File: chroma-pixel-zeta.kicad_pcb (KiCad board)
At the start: 4 copper layers, 138 x 93.2 mm, 181 parts, among them J10 Conn_01x24_MountingPin, J11 AudioJack3, J12 USB_A, J14 LCD_TP_I2C, J2 TFT_LCD, J3 2169900003, J4 SPI_LCD, J5 I2C-STEMMA-QT, J6 Micro_SD_Card_Det1, J7 swd, J8 SPKR, J9 UART, Q1 MMBT3904, Q2 MMBT3904, Q3 MMBT3904, SW1 SW_Push, SW2 SW_Push, SW3 SW_Push, SW4 SW_Push, U1 MT25Q, U10 PCM5102A, U11 TLV75733PDBV, U12 STMPS2141STR, U2 STM32H743IITx, U4 MT25Q, U5 TPS61169, U6 MAX98357AETE_, U7 CAT24C128, U8 TLV75733PDBV, U9 MT48LC16M16A2P, Y1 25MHz, Y2 32.768KHz

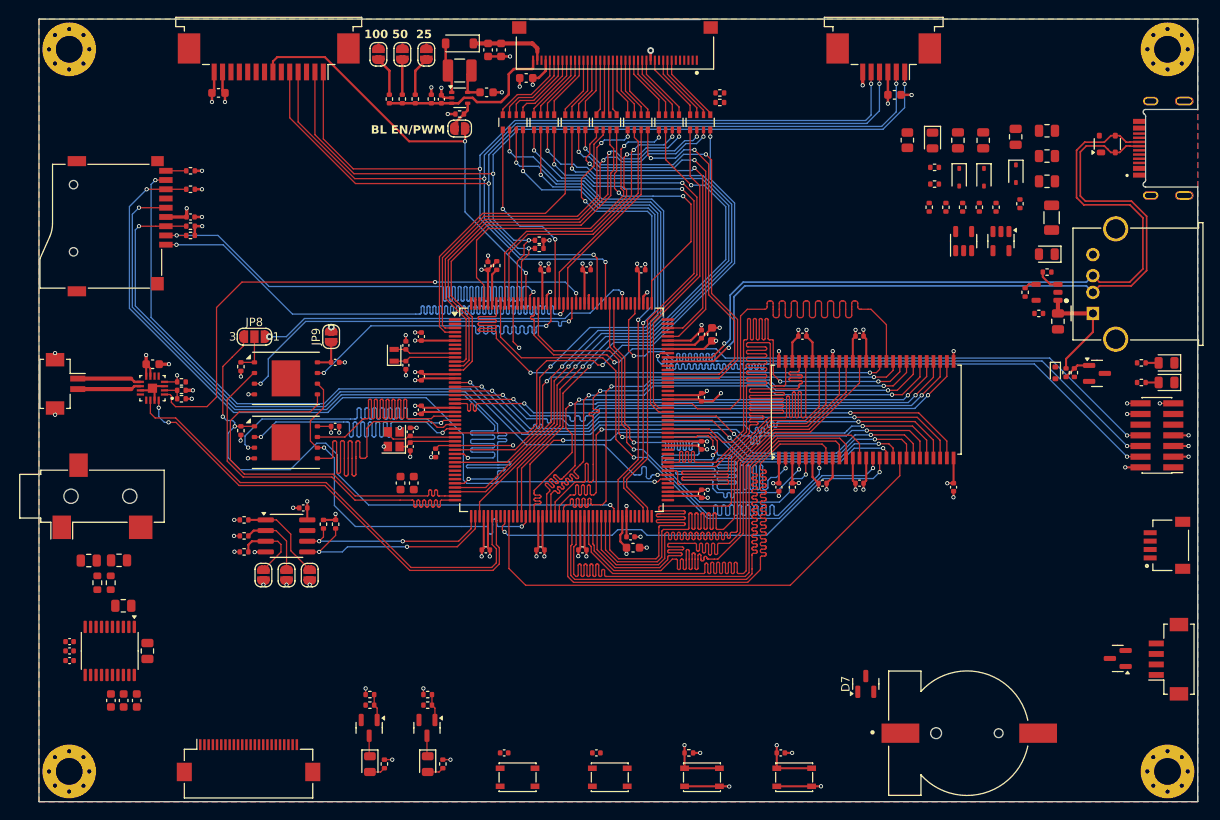
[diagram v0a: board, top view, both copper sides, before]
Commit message: Button, LED, i2s audio, LCD & SD ctrl left
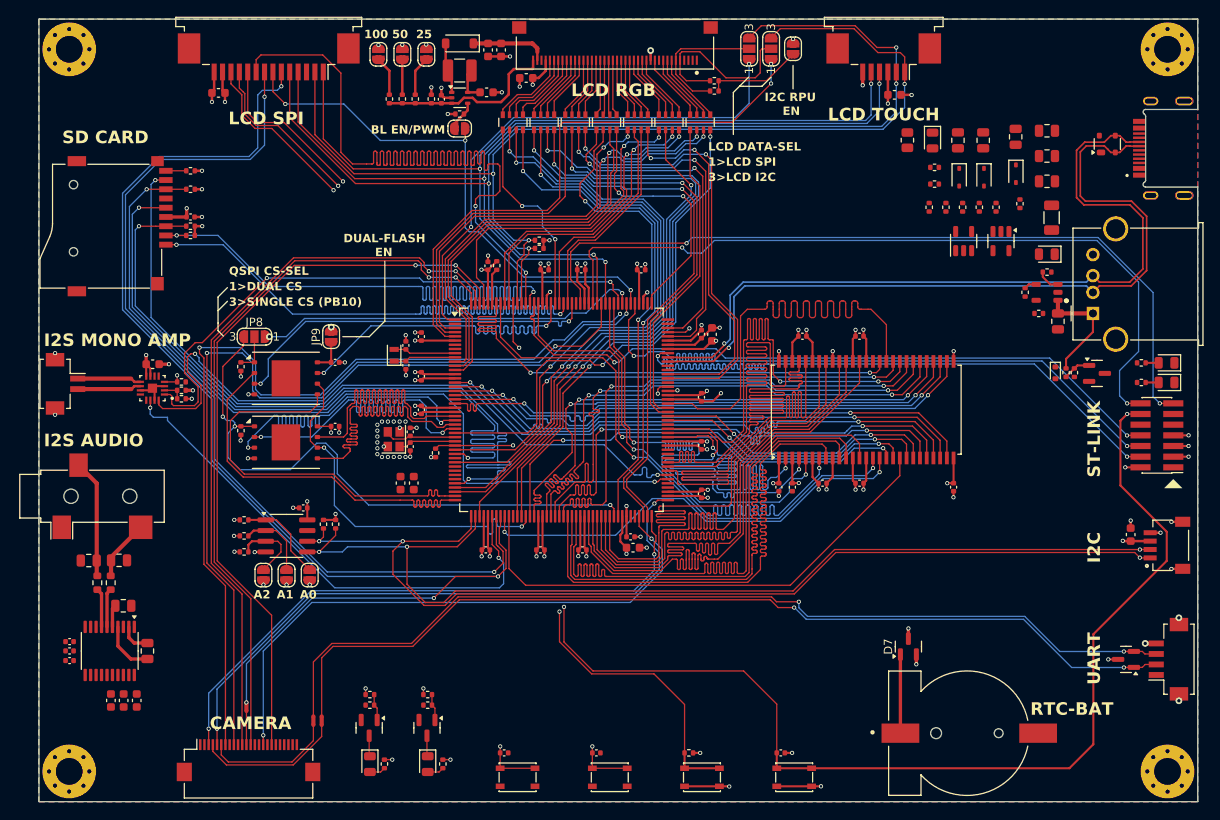
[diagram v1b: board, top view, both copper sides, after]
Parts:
- added C67: 10u, Capacitor_SMD:C_0603_1608Metric, F.Cu at (210.3, 108.4)
- added JP12: JMP, Jumper:SolderJumper-2_P1.3mm_Open_RoundedPad1.0x1.5mm, F.Cu at (170.1, 50.6)
- added JP13: LCD_DAT_SEL, Jumper:SolderJumper-3_P1.3mm_Open_RoundedPad1.0x1.5mm_NumberLabels, F.Cu at (167.4, 50.6)
- added JP14: LCD_CLK_SEL, Jumper:SolderJumper-3_P1.3mm_Open_RoundedPad1.0x1.5mm_NumberLabels, F.Cu at (164.8, 50.6)
- added NT1: NetTie_2, NetTie:NetTie-2_SMD_Pad0.5mm, F.Cu at (105.0, 128.9)
- added NT2: NetTie_2, NetTie:NetTie-2_SMD_Pad0.5mm, F.Cu at (112.9, 130.6)
- added NT3: NetTie_2, NetTie:NetTie-2_SMD_Pad0.5mm, F.Cu at (113.9, 130.6)
- moved D7 6.75 mm to (183.8, 121.8)
- moved R35 2.67 mm to (160.7, 54.4)
- moved D9 0.99 mm to (209.7, 123.3)
- moved R36 0.69 mm to (160.7, 55.6)
- moved C13 0.64 mm to (144.8, 76.9)
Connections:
- net /LCD/LCD_SCL renamed /LCD/LCD_CLK
- net /LCD/LCD_SDA renamed /LCD/LCD_DAT
- D9 pad 1: /IO/USART2_RX -> /IO/USART6_RX
- D9 pad 2: /IO/USART2_TX -> /IO/USART6_TX
- J10 pad 11: unconnected-(J10-Pin_11-Pad11) -> /DCMI/DCMI_D6
- J10 pad 12: /DCMI/DCMI_D7 -> /DCMI/DCMI_PIXCLK
- J10 pad 13: /DCMI/DCMI_PIXCLK -> /DCMI/DCMI_D7
- J10 pad 14: /DCMI/DCMI_D6 -> unconnected-(J10-Pin_14-Pad14)
- J10 pad 16: /DCMI/DCMI_D5 -> /DCMI/DCMI_HSYNC
- J10 pad 18: /DCMI/DCMI_D4 -> /DCMI/DCMI_VSYNC
- J10 pad 19: /DCMI/DCMI_D0 -> unconnected-(J10-Pin_19-Pad19)
- J10 pad 20: /DCMI/DCMI_D3 -> unconnected-(J10-Pin_20-Pad20)
- J10 pad 21: /DCMI/DCMI_D1 -> unconnected-(J10-Pin_21-Pad21)
- J10 pad 22: /DCMI/DCMI_D2 -> unconnected-(J10-Pin_22-Pad22)
- J10 pad 3: unconnected-(J10-Pin_3-Pad3) -> /DCMI/DCMI_D2
- J10 pad 4: unconnected-(J10-Pin_4-Pad4) -> /DCMI/DCMI_D1
- J10 pad 5: unconnected-(J10-Pin_5-Pad5) -> /DCMI/DCMI_D3
- J10 pad 6: unconnected-(J10-Pin_6-Pad6) -> /DCMI/DCMI_D0
- J10 pad 7: /DCMI/DCMI_VSYNC -> /DCMI/DCMI_D4
- J10 pad 9: /DCMI/DCMI_HSYNC -> /DCMI/DCMI_D5
- J4 pad 11: /LCD/LCD_RESET -> /LCD/LCD_SPI_RESET
- J9 pad 2: /IO/USART2_RX -> /IO/USART6_RX
- J9 pad 3: /IO/USART2_TX -> /IO/USART6_TX
- R31 pad 2: /MEMORY EEPROM/SDA -> /IO/STEMMA_SDA
- R32 pad 2: /MEMORY EEPROM/SCL -> /IO/STEMMA_SCL
- R35 pad 1: +3V3 -> Net-(JP12-A)
- R36 pad 1: +3V3 -> Net-(JP12-A)
- U2 pad 1: unconnected-(U2-PE2-Pad1) -> /LCD/LCD_SPI_CLK
- U2 pad 115: unconnected-(U2-PC6-Pad115) -> /IO/USART6_TX
- U2 pad 116: unconnected-(U2-PC7-Pad116) -> /IO/USART6_RX
- U2 pad 129: unconnected-(U2-PH14-Pad129) -> /MCU/DCMI_D4
- U2 pad 131: unconnected-(U2-PI0-Pad131) -> /LCD/LCD_DISP
- U2 pad 132: unconnected-(U2-PI1-Pad132) -> /LCD/LCD_CS
- U2 pad 138: /AUDIO/LRCK -> /LCD/LCD_BLK
- U2 pad 139: /AUDIO/BCK -> /AUDIO/I2S_CK
- U2 pad 141: unconnected-(U2-PC12-Pad141) -> /AUDIO/I2S_SDO
- U2 pad 145: unconnected-(U2-PD3-Pad145) -> /MCU/DCMI_D5
- U2 pad 147: unconnected-(U2-PD5-Pad147) -> /IO/DBG_TX
- U2 pad 150: unconnected-(U2-PD6-Pad150) -> /IO/DBG_RX
- U2 pad 151: /AUDIO/I2S_SDO -> /LCD/LCD_SPI_RESET
- U2 pad 163: /LCD/LCD_BLK -> /LCD/LCD_SDI(MOSI)
- U2 pad 174: unconnected-(U2-PI5-Pad174) -> /DCMI/DCMI_VSYNC
- U2 pad 175: unconnected-(U2-PI6-Pad175) -> /MCU/DCMI_D6
- U2 pad 176: unconnected-(U2-PI7-Pad176) -> /MCU/DCMI_D7
- U2 pad 2: unconnected-(U2-PE3-Pad2) -> /MCU/SD_DET
- U2 pad 45: /MEMORY EEPROM/SCL -> /IO/STEMMA_SCL
- U2 pad 46: /MEMORY EEPROM/SDA -> /IO/STEMMA_SDA
- U2 pad 5: unconnected-(U2-PE6-Pad5) -> /LCD/LCD_SPI_DAT
- U2 pad 51: /AUDIO/I2S_CK -> /LCD/LCD_SCK
- U2 pad 52: unconnected-(U2-PA6-Pad52) -> /LCD/LCD_SDO(MISO)
- U2 pad 7: unconnected-(U2-PI8-Pad7) -> /LCD/LCD_CS
- U2 pad 85: unconnected-(U2-PH8-Pad85) -> /DCMI/DCMI_HSYNC
- U2 pad 88: unconnected-(U2-PH11-Pad88) -> /MCU/DCMI_D2
- U2 pad 89: unconnected-(U2-PH12-Pad89) -> /MCU/DCMI_D3
- U7 pad 5: /MEMORY EEPROM/SDA -> /IO/STEMMA_SDA
- U7 pad 6: /MEMORY EEPROM/SCL -> /IO/STEMMA_SCL
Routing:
- net /IO/USART6_RX: track 0.00 -> 156.7 mm, vias 0 -> 3
- net /IO/USART6_TX: track 0.00 -> 153.4 mm, vias 0 -> 3
- net /LCD/LCD_SDO(MISO): track 0.00 -> 152.5 mm, vias 0 -> 4
- net /IO/STEMMA_SDA: track 0.00 -> 122.7 mm, vias 0 -> 3
- net /IO/STEMMA_SCL: track 0.00 -> 122.4 mm, vias 0 -> 3
- net /DCMI/DCMI_D4: track 0.00 -> 119.6 mm, vias 0 -> 3
- net /LCD/LCD_SDI(MOSI): track 0.00 -> 116.6 mm, vias 0 -> 2
- net /LCD/LCD_SCK: track 0.00 -> 109.9 mm, vias 0 -> 2
- net /DCMI/DCMI_D5: track 0.00 -> 105.3 mm, vias 0 -> 2
- net /IO/DBG_RX: track 1.63 -> 94.6 mm, vias 1 -> 2
- net VBAT: track 4.75 -> 96.6 mm, vias 1 -> 2
- net /IO/DBG_TX: track 1.61 -> 92.3 mm, vias 1 -> 2
- net /DCMI/DCMI_D6: track 0.00 -> 88.6 mm, vias 0 -> 2
- net /DCMI/DCMI_VSYNC: track 0.00 -> 88.5 mm, vias 0 -> 2
- net /DCMI/DCMI_D7: track 0.00 -> 87.7 mm, vias 0 -> 2
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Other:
- board text added: "1>DUAL CS"
- board text added: "1>LCD SPI"
- board text added: "3>LCD I2C"
- board text added: "3>SINGLE CS (PB10)"
- board text added: "3V3"
- board text added: "5V"
- board text added: "A0"
- board text added: "A1"
- board text added: "A2"
- board text added: "CAMERA"
- board text added: "DUAL-FLASH"
- board text added: "EN"
- board text added: "GND"
- board text added: "I2C"
- board text added: "I2C RPU"
- board text added: "I2S AUDIO"
- board text added: "I2S MONO AMP"
- board text added: "LCD DATA-SEL"
- board text added: "LCD RGB"
- board text added: "LCD SPI"
- board text added: "LCD TOUCH"
- board text added: "QSPI CS-SEL"
- board text added: "RTC-BAT"
- board text added: "RX"
- board text added: "SCL"
- board text added: "SD CARD"
- board text added: "SDA"
- board text added: "ST-LINK"
- board text added: "TX"
- board text added: "UART"

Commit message: Almost finished
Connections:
- J4 pad 12: /LCD/LCD_CS -> /LCD/LCD_SPI_CS
- U2 pad 134: unconnected-(U2-PI3-Pad134) -> /LCD/LCD_DC
- U2 pad 7: /LCD/LCD_CS -> /LCD/LCD_SPI_CS
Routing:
- net /LCD/LCD_SPI_CS: track 0.00 -> 89.1 mm, vias 0 -> 2
- net /LCD/LCD_DC: track 19.6 -> 73.7 mm, vias 1 -> 2
- net /MCU/SD_DET: track 2.42 -> 51.7 mm, vias 0 -> 4
- net /LCD/LCD_DISP: track 0.00 -> 44.4 mm, vias 0 -> 2
- net /LCD/LCD_SPI_RESET: track 19.9 -> 58.7 mm, vias 1 -> 2
- net /LCD/LCD_CS: track 20.3 -> 56.9 mm, vias 1 -> 2
- net /MCU/QUADSPI_BK2_IO3: track 44.7 -> 33.2 mm
- net /LCD/LTDC_HSYNC: track 55.6 -> 56.8 mm
- net /LCD/LTDC_VSYNC: track 55.4 -> 56.6 mm
- net /LCD/LTDC_G6: track 46.4 -> 47.6 mm
- net /IO/DBG_TX: track 92.3 -> 93.5 mm
- net /IO/STEMMA_SDA: track 122.7 -> 123.8 mm
- net /LCD/LCD_BLK: track 63.8 -> 64.9 mm
- net /LCD/LCD_SPI_DAT: track 68.4 -> 69.5 mm
- net GND: track 139.9 -> 140.9 mm
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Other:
- board text added: "BOOT0"
- board text added: "BTN0"
- board text added: "BTN1"
- board text added: "LED0"
- board text added: "LED1"
- board text added: "RESET"

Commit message: Still on progress...
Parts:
- removed C45: 10uF/0805, Capacitor_SMD:C_0805_2012Metric
- removed D3: NSR0320MW2T1G, Diode_SMD:D_SOD-323
- removed R22: 100K, Resistor_SMD:R_0402_1005Metric
- removed R40: 10K, Resistor_SMD:R_0402_1005Metric
- removed U11: TLV75733PDBV, Package_TO_SOT_SMD:SOT-23-5
- added C68: 100n, Capacitor_SMD:C_0402_1005Metric, F.Cu at (90.3, 127.3)
- added U13: AMS1117-3.3, Package_TO_SOT_SMD:SOT-223-3_TabPin2, F.Cu at (193.2, 63.1)
- J10: footprint Connector_FFC-FPC:Hirose_FH12-24S-0.5SH_1x24-1MP_P0.50mm_Horizontal -> Connector_FFC-FPC:Jushuo_AFC07-S24FCA-00_1x24-1MP_P0.50_Horizontal
- J11: footprint Connector_Audio:Jack_3.5mm_CUI_SJ-3523-SMT_Horizontal -> Audio-jack-3_5mm-custom:XKB-PJ-320B-SMT
- R16: value NC -> 100K
- moved D10 44.2 mm to (214.3, 104.5), turned to 0 degrees
- moved R13 25.0 mm to (207.0, 52.4), turned to 90 degrees
- moved D4 22.5 mm to (182.5, 61.2)
- moved C30 21.2 mm to (182.5, 71.9)
- moved C43 20.2 mm to (209.4, 52.4), turned to 90 degrees
- moved C44 17.8 mm to (182.5, 64.4)
- moved R39 16.1 mm to (202.4, 58.9), turned to 180 degrees
- moved R12 13.9 mm to (207.1, 64.2), turned to 0 degrees
- moved R11 13.6 mm to (207.0, 59.7), turned to 180 degrees
- moved C56 12.1 mm to (85.4, 117.1), turned to 90 degrees
- moved C55 10.5 mm to (93.6, 119.4), turned to 0 degrees
- moved R20 10.2 mm to (182.1, 70.3), turned to 0 degrees
- moved C54 10.2 mm to (93.9, 118.2), turned to 0 degrees
- moved C59 9.85 mm to (91.6, 127.3), turned to -90 degrees
- moved U8 9.77 mm to (182.5, 67.6)
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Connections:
- net /AUDIO/I2S_CK renamed /AUDIO/I2S3_CK
- net /AUDIO/I2S_SDO renamed /AUDIO/I2S3_SDO
- net /AUDIO/I2S_WS renamed /AUDIO/I2S3_WS
- C62 pad 1: +3V3 -> +3V3A
- C64 pad 1: +3V3 -> +3V3A
- C65 pad 1: +3V3 -> +3V3A
- C66 pad 1: LCD_VDD -> +3V3A
- J10 pad 20: unconnected-(J10-Pin_20-Pad20) -> /IO/STEMMA_SCL
- J10 pad 22: unconnected-(J10-Pin_22-Pad22) -> /IO/STEMMA_SDA
- J14 pad 3: +3V3 -> +3V3A
- J2 pad 37: +3V3 -> +3V3A
- J4 pad 14: LCD_VDD -> +3V3A
- NT2 pad 2: /MCU/DCMI_D0 -> /DCMI/DCMI_D0
- NT3 pad 2: /MCU/DCMI_D1 -> /DCMI/DCMI_D1
- R14 pad 1: /AUDIO/I2S_SD_MODE -> /AUDIO/I2S3_SD_MODE
- R41 pad 1: +3V3 -> +3V3A
- U10 pad 10: unconnected-(U10-DEMP-Pad10) -> GND
- U10 pad 11: unconnected-(U10-FLT-Pad11) -> GND
- U10 pad 12: unconnected-(U10-SCK-Pad12) -> GND
- U10 pad 13: /AUDIO/BCK -> /AUDIO/I2S2_CK
- U10 pad 14: /AUDIO/DIN -> /AUDIO/I2S2_DIN
- U10 pad 15: /AUDIO/LRCK -> /AUDIO/I2S2_WS
- U10 pad 16: unconnected-(U10-FMT-Pad16) -> GND
- U10 pad 17: unconnected-(U10-XSMT-Pad17) -> +3V3
- U10 pad 18: unconnected-(U10-LDOO-Pad18) -> Net-(U10-LDOO)
- U2 pad 100: /AUDIO/DIN -> /MCU/DO
- U2 pad 121: unconnected-(U2-PA10-Pad121) -> /LCD/LCD_DC
- U2 pad 129: /MCU/DCMI_D4 -> /DCMI/DCMI_D4
- U2 pad 134: /LCD/LCD_DC -> /AUDIO/I2S2_DIN
- U2 pad 145: /MCU/DCMI_D5 -> /DCMI/DCMI_D5
- U2 pad 175: /MCU/DCMI_D6 -> /DCMI/DCMI_D6
- U2 pad 176: /MCU/DCMI_D7 -> /DCMI/DCMI_D7
- U2 pad 34: unconnected-(U2-PC2_C-Pad34) -> /AUDIO/I2S3_SD_MODE
- U2 pad 55: unconnected-(U2-PC5-Pad55) -> /MCU/LED_0
- U2 pad 83: unconnected-(U2-PH6-Pad83) -> /MCU/LED_1
- U2 pad 84: unconnected-(U2-PH7-Pad84) -> /MCU/BTN1
- U2 pad 88: /MCU/DCMI_D2 -> /DCMI/DCMI_D2
- U2 pad 89: /MCU/DCMI_D3 -> /DCMI/DCMI_D3
- U2 pad 92: unconnected-(U2-PB12-Pad92) -> /AUDIO/I2S2_WS
- U2 pad 93: unconnected-(U2-PB13-Pad93) -> /AUDIO/I2S2_CK
- U2 pad 99: unconnected-(U2-PD11-Pad99) -> /MCU/BTN0
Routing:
- net +3V3A: track 0.00 -> 403.7 mm, vias 0 -> 13
- net VDD: track 18.2 -> 231.1 mm, vias 2 -> 15
- net /AUDIO/I2S2_WS: track 0.00 -> 104.3 mm, vias 0 -> 4
- net /AUDIO/I2S2_CK: track 0.00 -> 104.0 mm, vias 0 -> 4
- net /AUDIO/I2S2_DIN: track 0.00 -> 102.5 mm, vias 0 -> 4
- net /MCU/BTN1: track 6.75 -> 64.8 mm, vias 1 -> 2
- net /AUDIO/I2S3_SD_MODE: track 0.00 -> 47.0 mm, vias 0 -> 2
- net /MCU/LED_1: track 0.74 -> 46.3 mm, vias 1 -> 2
- net /MCU/BTN0: track 6.75 -> 50.2 mm, vias 1 -> 2
- net /MCU/LED_0: track 0.74 -> 40.1 mm, vias 1 -> 2
- net /LCD/LCD_DC: track 73.7 -> 105.8 mm
- net /IO/STEMMA_SCL: track 122.4 -> 150.6 mm
- net /IO/STEMMA_SDA: track 123.8 -> 150.7 mm
- net GND: track 140.9 -> 166.3 mm, vias 89 -> 107
- net VBUS: track 0.00 -> 25.1 mm, vias 0 -> 5
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- added copper zone on F.Cu, net +3V3
- added copper zone on B.Cu, net +3V3A
- added copper zone on F.Cu, net +3V3A
- added copper zone on In2.Cu, net +3V3A
- added copper zone on F.Cu, net VDD
- added copper zone on In2.Cu, net VDD
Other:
- outline, holes or cut-outs redrawn
